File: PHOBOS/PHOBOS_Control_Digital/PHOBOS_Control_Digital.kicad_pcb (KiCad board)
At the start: 2 copper layers, 34.7 x 49.9 mm, 61 parts, among them IC1 MAPS-010144-TR0500, J10 PS4, J11 PWR, J2 RF_OUT, J3 USB4056-03-A_REVA2, J4 Screw_Terminal_01x02, J6 PS1, J7 PS2, J8 Conn_01x02, J9 PS3, U1 SX1280IMLTRT, U2 W25Q128JVSIQ, U3 NCP1117-3.3_SOT223, U4 RP2040, Y1 C1E-52.000-10-1012-X-M, Y2 ABM8-272-T3

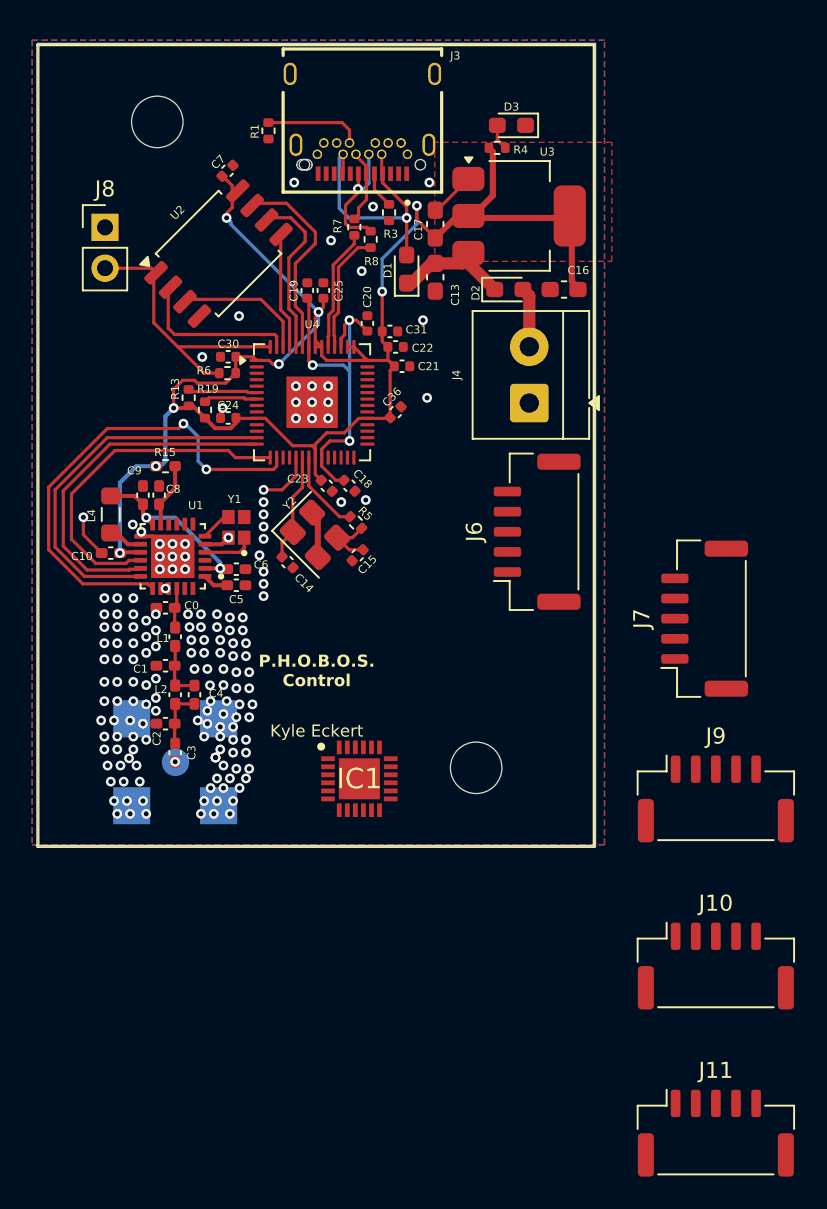
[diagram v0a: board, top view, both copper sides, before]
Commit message: connectors fine tuned (JST-GH 10 pin). 3v Inverter added. Needs routing
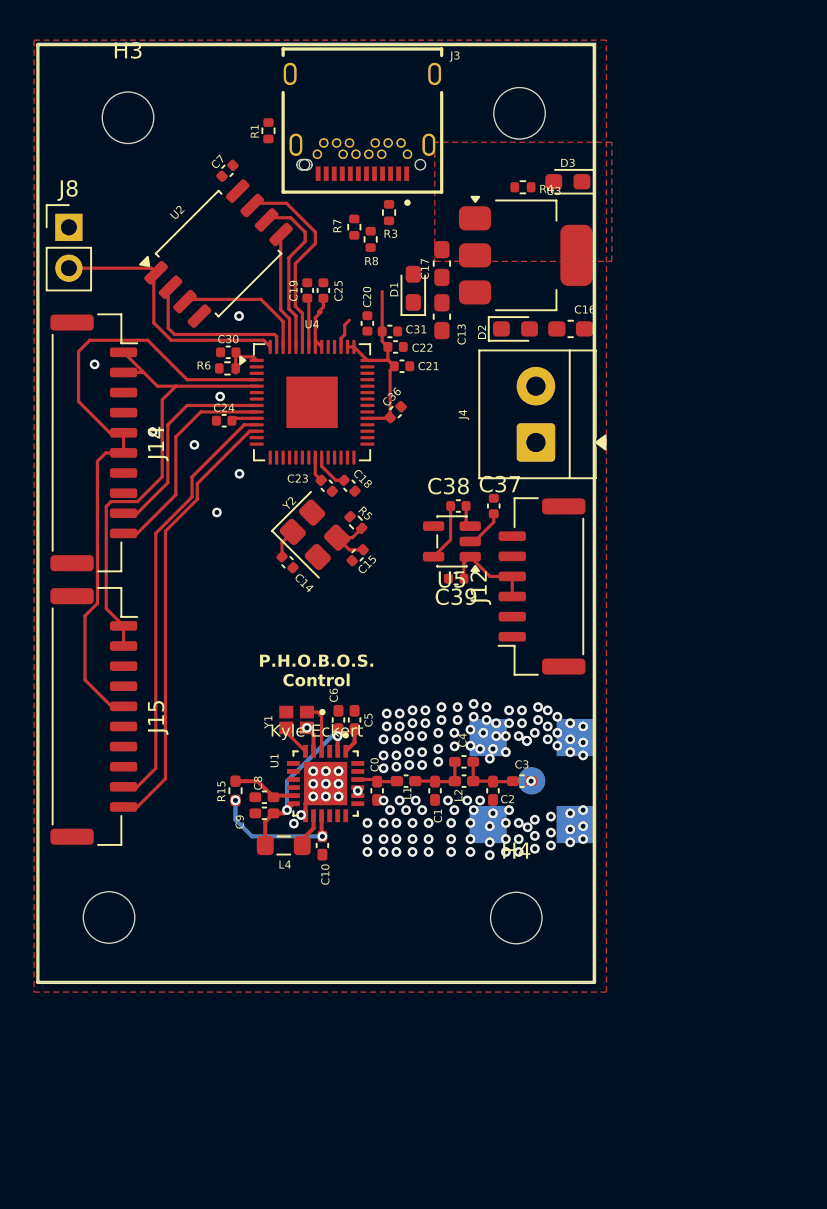
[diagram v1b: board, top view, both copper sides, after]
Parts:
- removed IC1: MAPS-010144-TR0500, MAPS-010144-TR0500:QFN50P400X400X100-25N-D
- removed J10: PS4, Connector_JST:JST_GH_SM05B-GHS-TB_1x05-1MP_P1.25mm_Horizontal
- removed J11: PWR, Connector_JST:JST_GH_SM05B-GHS-TB_1x05-1MP_P1.25mm_Horizontal
- removed J6: PS1, Connector_JST:JST_GH_SM05B-GHS-TB_1x05-1MP_P1.25mm_Horizontal
- removed J7: PS2, Connector_JST:JST_GH_SM05B-GHS-TB_1x05-1MP_P1.25mm_Horizontal
- removed J9: PS3, Connector_JST:JST_GH_SM05B-GHS-TB_1x05-1MP_P1.25mm_Horizontal
- removed R13, R19: 4.7k, Resistor_SMD:R_0402_1005Metric
- added C37: 1u, Capacitor_SMD:C_0402_1005Metric, F.Cu at (168.6, 105.7)
- added C38: 1u, Capacitor_SMD:C_0402_1005Metric, F.Cu at (166.4, 105.7)
- added C39: 1u, Capacitor_SMD:C_0402_1005Metric, F.Cu at (166.3, 110.2)
- added H3: MountingHole, MountingHole:MountingHole_3.2mm_M3, F.Cu at (145.9, 81.6)
- added H4: MountingHole, MountingHole:MountingHole_3.2mm_M3, F.Cu at (170.0, 131.3)
- added J12: PWR, Connector_JST:JST_GH_SM06B-GHS-TB_1x06-1MP_P1.25mm_Horizontal, F.Cu at (171.6, 110.7)
- added J14: PS1-2, Connector_JST:JST_GH_SM10B-GHS-TB_1x10-1MP_P1.25mm_Horizontal, F.Cu at (143.8, 101.8)
- added J15: PS3-4, Connector_JST:JST_GH_SM10B-GHS-TB_1x10-1MP_P1.25mm_Horizontal, F.Cu at (143.8, 118.8)
- added U5: TPS60403DBV, Package_TO_SOT_SMD:SOT-23-5, F.Cu at (166.0, 107.9)
- moved H2 24.6 mm to (144.7, 131.3)
- moved L4 23.2 mm to (155.6, 126.8), turned to 180 degrees
- moved H1 22.5 mm to (170.2, 81.3)
- moved C10 22.4 mm to (158.0, 126.8), turned to -90 degrees
- moved J2 22.2 mm to (171.0, 122.8), turned to 180 degrees
- moved C3 21.6 mm to (170.4, 122.8), turned to 0 degrees
- moved C9 21.2 mm to (154.4, 124.8), turned to 180 degrees
- moved C2 20.8 mm to (168.6, 123.4), turned to -90 degrees
- moved R15 20.6 mm to (152.6, 123.4), turned to -90 degrees
- moved C8 19.9 mm to (154.4, 123.8), turned to 180 degrees
- moved L2 18.7 mm to (166.8, 122.8), turned to 0 degrees
- moved C1 18.5 mm to (165.0, 123.4), turned to -90 degrees
- moved C0 17.4 mm to (161.4, 123.4), turned to -90 degrees
- moved C4 17.3 mm to (166.8, 121.6), turned to 0 degrees
- moved U1 17.0 mm to (158.2, 122.9), turned to -90 degrees
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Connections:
- U4 pad 11: /GPIO8 -> /LE3
- U4 pad 12: /GPIO9 -> /LE4
- U4 pad 4: unconnected-(U4-GPIO2-Pad4) -> /SCK
- U4 pad 5: unconnected-(U4-GPIO3-Pad5) -> /MOSI
- U4 pad 8: unconnected-(U4-GPIO6-Pad8) -> /LE1
- U4 pad 9: /GPIO7 -> /LE2
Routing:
- net +3V3: track 102.5 -> 33.2 mm, vias 8 -> 2
- net /SCK: track 0.00 -> 39.2 mm
- net /NSS_TRANS: track 29.8 -> 0.00 mm, vias 2 -> 0
- net /MOSI: track 0.00 -> 29.7 mm
- net /LE4: track 0.00 -> 27.5 mm
- net /LE3: track 0.00 -> 26.9 mm
- net /SCK_TRANS: track 23.5 -> 0.00 mm
- net /MOSI_TRANS: track 22.1 -> 0.00 mm
- net /MISO_TRANS: track 21.5 -> 0.00 mm
- net VBUS: track 16.0 -> 0.00 mm, vias 1 -> 0
- net +1V1: track 22.3 -> 7.22 mm, vias 3 -> 0
- net /LE2: track 0.00 -> 13.5 mm
- net /LE1: track 0.00 -> 13.2 mm
- net GND: track 16.8 -> 4.15 mm, vias 165 -> 141
- net /USB_D-: track 7.83 -> 0.00 mm, vias 1 -> 0
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- added copper zone on In2.Cu, net +3V3
- added copper zone on In1.Cu, net GND
- removed copper zone on B.Cu, net GND
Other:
- board size 34.7 x 49.9 mm -> 34.7 x 58.3 mm
- copper layers 2 -> 4

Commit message: Centered and nicer layout.
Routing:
- net /QSPI_SS: track 16.6 -> 0.00 mm
- net /QSPI_SD3: track 12.5 -> 0.00 mm
- net /QSPI_SCLK: track 10.5 -> 0.00 mm
- net /QSPI_SD1: track 10.2 -> 0.00 mm
- net /QSPI_SD2: track 8.30 -> 0.00 mm
- net /QSPI_SD0: track 7.21 -> 0.00 mm
- net +3V3: track 33.2 -> 30.4 mm
- net GND: vias 141 -> 140

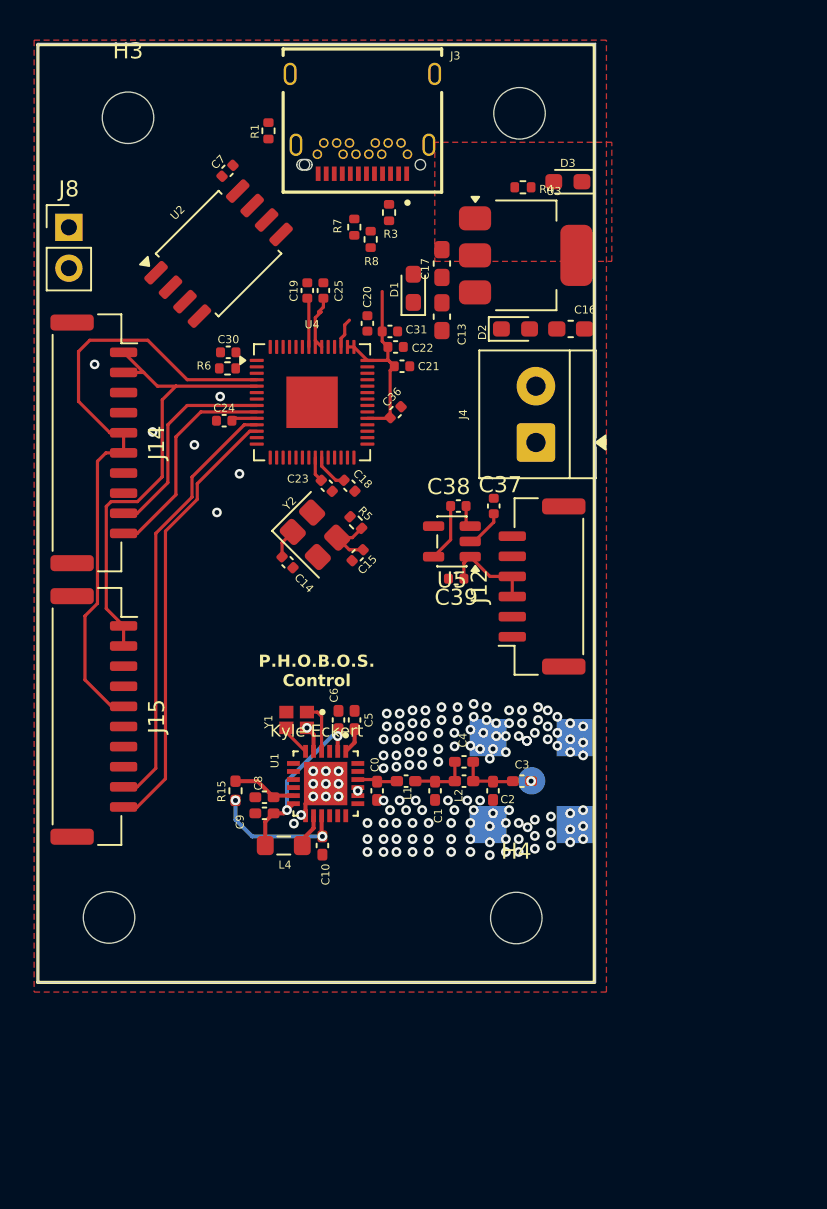
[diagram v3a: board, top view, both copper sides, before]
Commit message: Re-Centered. M3 bolt model added. SMA shifted to top side. Hole zones redone.
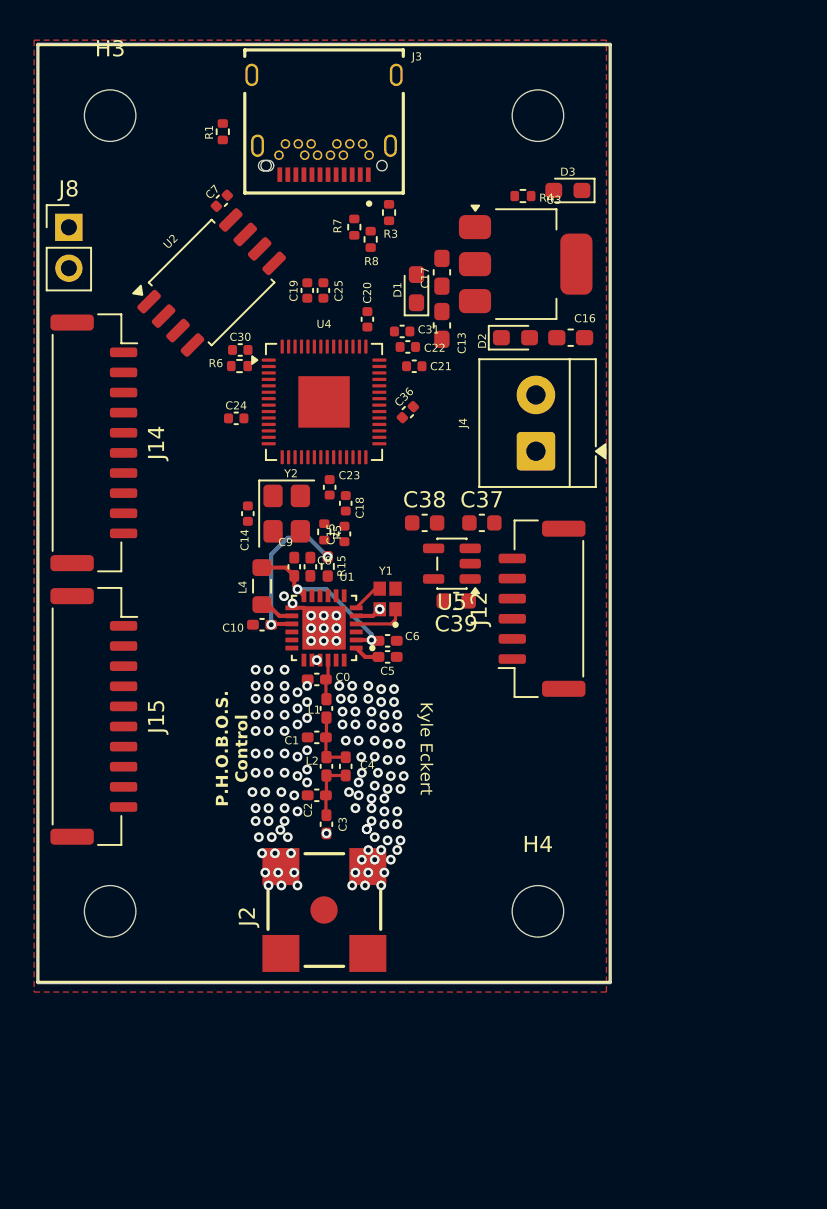
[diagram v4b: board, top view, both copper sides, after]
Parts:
- C37, C38, C39: footprint Capacitor_SMD:C_0402_1005Metric -> Capacitor_SMD:C_0603_1608Metric
- J2: moved to F.Cu
- moved L4 16.2 mm to (154.2, 110.7), turned to 90 degrees
- moved C9 15.4 mm to (156.2, 109.5), turned to 90 degrees
- moved J2 15.2 mm to (158.1, 130.8), turned to 90 degrees
- moved R15 15.1 mm to (158.3, 109.5), turned to 90 degrees
- moved C8 14.6 mm to (157.2, 109.5), turned to 90 degrees
- moved C10 14.2 mm to (154.2, 113.1), turned to 180 degrees
- moved C3 12.4 mm to (158.2, 125.5), turned to -90 degrees
- moved C2 11.0 mm to (157.6, 123.7), turned to 180 degrees
- moved U1 9.67 mm to (158.1, 113.3), turned to 180 degrees
- moved Y1 9.41 mm to (162.0, 111.5), turned to 90 degrees
- moved L2 8.60 mm to (158.2, 121.9), turned to -90 degrees
- moved C1 8.06 mm to (157.6, 120.1), turned to 180 degrees
- moved C0 7.87 mm to (157.6, 116.5), turned to 180 degrees
- moved C4 7.35 mm to (159.4, 121.9), turned to -90 degrees
- moved L1 6.70 mm to (158.2, 118.3), turned to -90 degrees
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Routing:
- net /SCK: track 39.2 -> 0.00 mm
- net /MOSI: track 29.7 -> 0.00 mm
- net /LE4: track 27.5 -> 0.00 mm
- net /LE3: track 26.9 -> 0.00 mm
- net +3V3: track 30.4 -> 10.1 mm
- net /LE2: track 13.5 -> 0.00 mm
- net /LE1: track 13.2 -> 0.00 mm
- net +1V1: track 7.22 -> 0.00 mm
- net -3V3: track 5.90 -> 0.00 mm
- net /VBAT_IO: track 4.05 -> 0.00 mm
- net Net-(C15-Pad1): track 3.68 -> 0.00 mm
- net Net-(U5-C_{FLY+}): track 3.59 -> 0.00 mm
- net /XIN: track 1.82 -> 0.00 mm
- net Net-(U5-C_{FLY-}): track 1.36 -> 0.00 mm
- net GND: vias 140 -> 134
- removed copper zone on F.Cu, net +3V3
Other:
- board size 34.7 x 58.3 mm -> 35.6 x 58.4 mm

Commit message: Routing Began
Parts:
- moved R8 1.15 mm to (160.1, 88.4)
- moved R7 0.99 mm to (159.0, 88.4)
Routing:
- net /SCK: track 0.00 -> 38.6 mm
- net /MOSI: track 0.00 -> 29.6 mm
- net /LE4: track 0.00 -> 28.9 mm
- net /LE3: track 0.00 -> 28.2 mm
- net /NSS_TRANS: track 0.00 -> 20.5 mm, vias 0 -> 2
- net /SCK_TRANS: track 0.00 -> 19.6 mm
- net /MOSI_TRANS: track 0.00 -> 17.7 mm
- net /MISO_TRANS: track 0.00 -> 16.1 mm
- net /LE2: track 0.00 -> 13.7 mm
- net /LE1: track 0.00 -> 13.5 mm
- net VIN: track 0.00 -> 7.08 mm
- net /XIN: track 0.00 -> 5.64 mm
- net /XOUT: track 0.00 -> 4.22 mm
- net Net-(U5-C_{FLY+}): track 0.00 -> 4.04 mm
- net +BATT: track 0.00 -> 3.72 mm
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
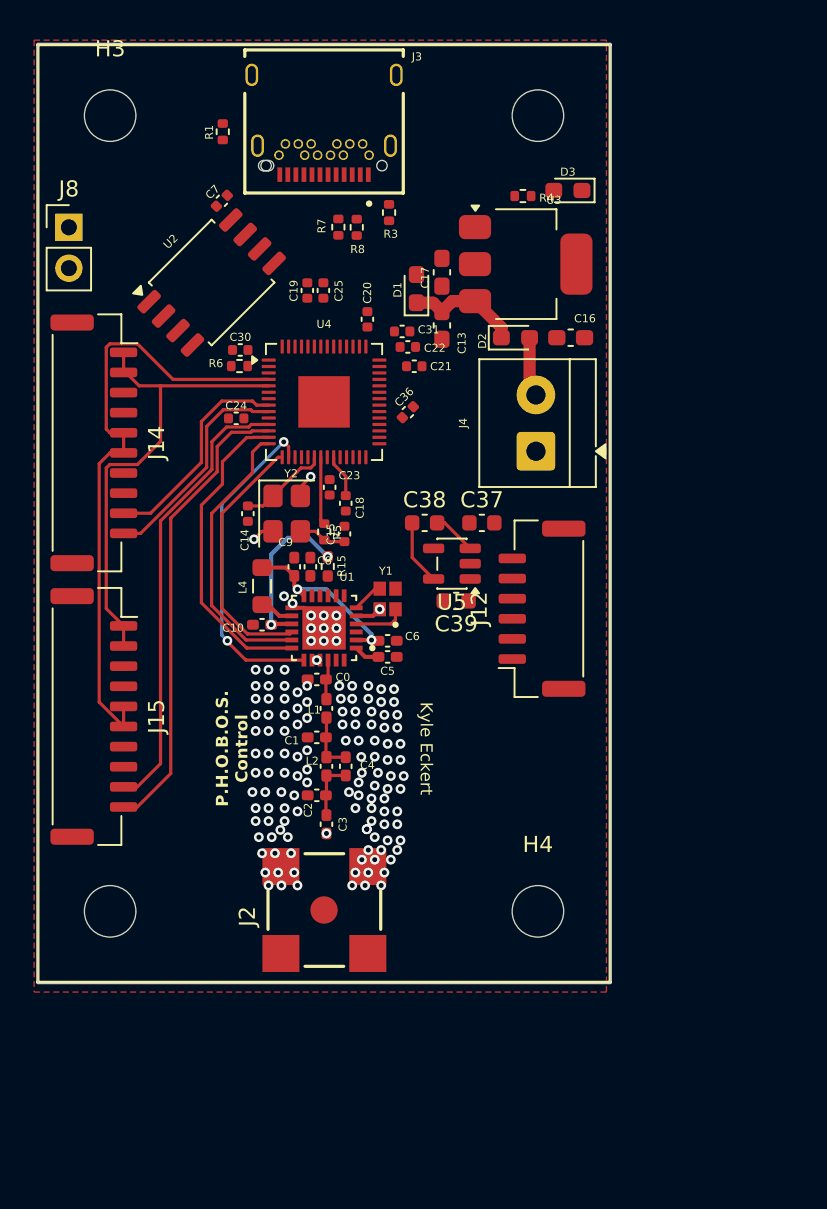
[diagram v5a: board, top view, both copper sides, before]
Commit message: Routing complete. DRC errors with USB (Check USB Routing), check silkscreen warnings
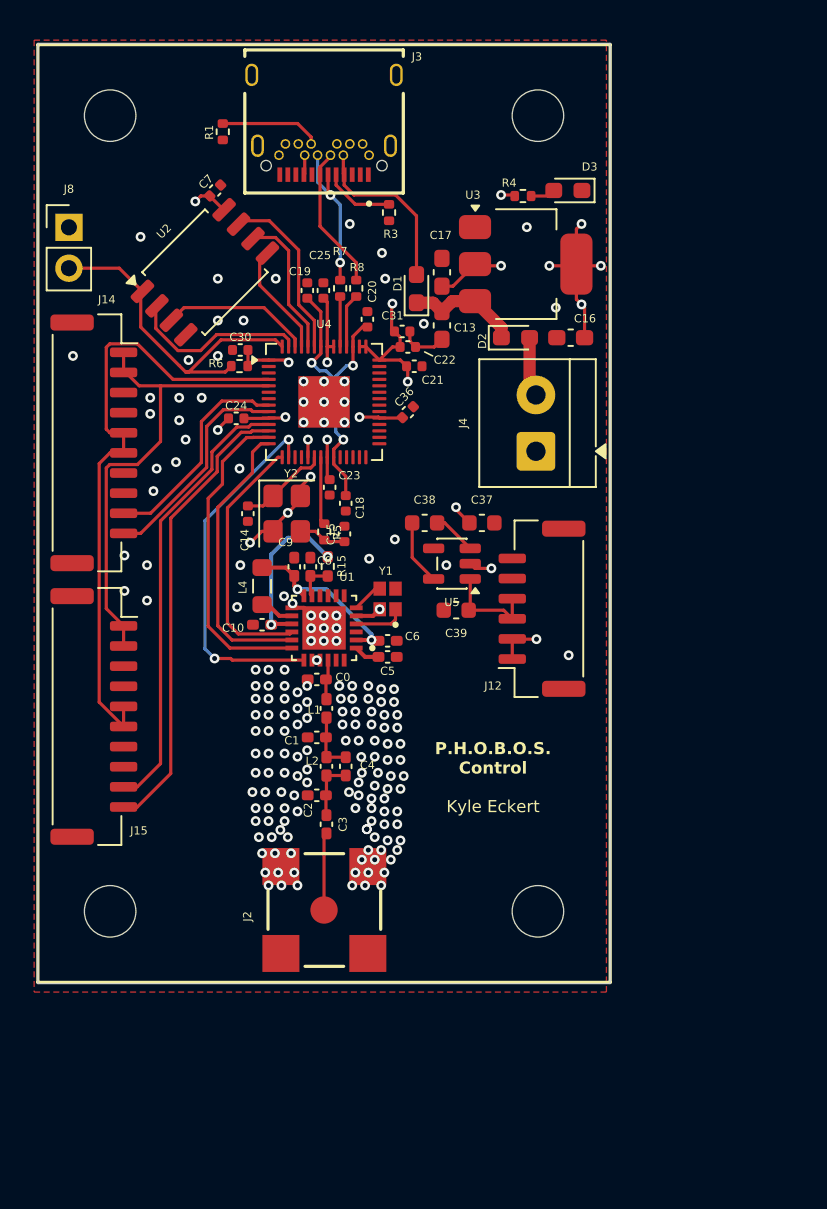
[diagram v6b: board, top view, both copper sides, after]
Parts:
- moved R7 3.80 mm to (159.1, 92.2)
- moved R8 3.79 mm to (160.1, 92.2)
- moved C7 0.76 mm to (151.3, 86.1)
- moved U2 0.76 mm to (150.7, 91.2)
- moved C39 0.58 mm to (166.3, 112.2)
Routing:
- net +3V3: track 10.1 -> 58.8 mm, vias 2 -> 19
- net /QSPI_SS: track 0.00 -> 21.4 mm
- net +1V1: track 2.69 -> 19.9 mm, vias 0 -> 3
- net VBUS: track 0.00 -> 12.0 mm
- net /QSPI_SD1: track 0.00 -> 11.2 mm
- net /QSPI_SD3: track 0.00 -> 11.0 mm
- net /USB_D+: track 0.00 -> 9.67 mm, vias 0 -> 2
- net /QSPI_SD2: track 0.00 -> 9.30 mm
- net /QSPI_SCLK: track 0.00 -> 9.04 mm
- net /USB_D-: track 0.00 -> 8.96 mm
- net GND: track 6.99 -> 15.3 mm, vias 136 -> 182
- net /QSPI_SD0: track 0.00 -> 7.09 mm
- net Net-(J3-CC2): track 0.00 -> 6.27 mm
- net -3V3: track 0.00 -> 6.16 mm
- net /ANTENNA: track 0.00 -> 4.82 mm, vias 1 -> 0
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- added copper zone on In2.Cu, net VBUS
